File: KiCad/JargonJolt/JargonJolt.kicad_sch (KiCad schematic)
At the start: 0 parts

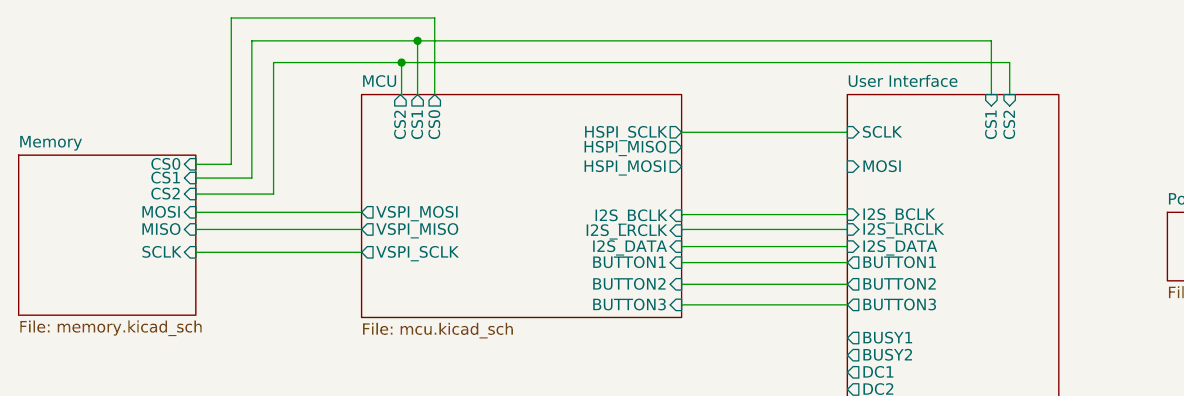
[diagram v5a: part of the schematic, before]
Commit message: added sd module + fixed CS pins
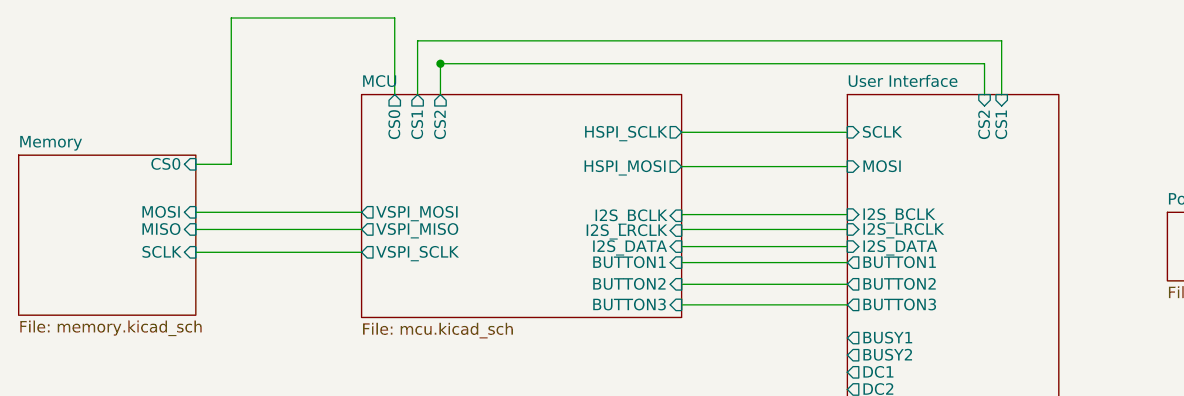
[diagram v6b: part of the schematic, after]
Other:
- sheet MCU ports: added none; removed HSPI_MISO
- sheet Memory ports: added none; removed CS1, CS2
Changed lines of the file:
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@@
 (kicad_sch (version 20230121) (generator eeschema)
   (paper "A4")
-  (junction (at 104.14 80.518) (diameter 0) (color 0 0 0 0)
-  )
-  (junction (at 105.918 78.105) (diameter 0) (color 0 0 0 0)
+  (junction (at 108.458 80.645) (diameter 0) (color 0 0 0 0)
   )
   (wire (pts (xy 135.255 97.409) (xy 153.67 97.409))
     (stroke (width 0) (type default))
   )
-  (wire (pts (xy 104.14 84.074) (xy 104.013 84.074))
+  (wire (pts (xy 108.458 80.645) (xy 108.458 84.074))
+    (stroke (width 0) (type default))
+  )
+  (wire (pts (xy 108.458 80.518) (xy 108.458 80.645))
+    (stroke (width 0) (type default))
+  )
+  (wire (pts (xy 135.255 92.075) (xy 153.67 92.075))
     (stroke (width 0) (type default))
   )
@@
     (stroke (width 0) (type default))
   )
-  (wire (pts (xy 89.916 80.518) (xy 89.916 95.123))
+  (wire (pts (xy 168.91 80.645) (xy 108.458 80.645))
     (stroke (width 0) (type default))
   )
@@
     (stroke (width 0) (type default))
   )
-  (wire (pts (xy 104.14 80.518) (xy 104.14 84.074))
-    (stroke (width 0) (type default))
-  )
   (wire (pts (xy 135.255 99.06) (xy 135.255 99.187))
     (stroke (width 0) (type default))
   )
-  (wire (pts (xy 87.503 93.345) (xy 81.28 93.345))
-    (stroke (width 0) (type default))
-  )
-  (wire (pts (xy 107.823 75.565) (xy 107.823 84.074))
+  (wire (pts (xy 103.378 75.565) (xy 103.378 84.074))
     (stroke (width 0) (type default))
   )
@@
     (stroke (width 0) (type default))
   )
+  (wire (pts (xy 168.91 80.645) (xy 168.91 84.074))
+    (stroke (width 0) (type default))
+  )
   (wire (pts (xy 135.255 99.06) (xy 153.67 99.06))
     (stroke (width 0) (type default))
   )
-  (wire (pts (xy 104.14 80.518) (xy 89.916 80.518))
-    (stroke (width 0) (type default))
-  )
-  (wire (pts (xy 169.672 84.074) (xy 169.672 78.105))
-    (stroke (width 0) (type default))
-  )
-  (wire (pts (xy 89.916 95.123) (xy 81.28 95.123))
+  (wire (pts (xy 170.815 84.074) (xy 170.815 78.105))
     (stroke (width 0) (type default))
   )
@@
     (stroke (width 0) (type default))
   )
-  (wire (pts (xy 169.672 78.105) (xy 105.918 78.105))
+  (wire (pts (xy 170.815 78.105) (xy 105.918 78.105))
     (stroke (width 0) (type default))
   )
@@
     (stroke (width 0) (type default))
   )
-  (wire (pts (xy 87.503 78.105) (xy 87.503 93.345))
-    (stroke (width 0) (type default))
-  )
-  (wire (pts (xy 105.918 78.105) (xy 87.503 78.105))
-    (stroke (width 0) (type default))
-  )
   (wire (pts (xy 135.255 102.743) (xy 153.67 102.743))
     (stroke (width 0) (type default))
   )
-  (wire (pts (xy 107.823 75.565) (xy 85.217 75.565))
-    (stroke (width 0) (type default))
-  )
-  (wire (pts (xy 171.704 84.074) (xy 171.704 80.518))
+  (wire (pts (xy 103.378 75.565) (xy 85.217 75.565))
     (stroke (width 0) (type default))
   )
@@
   )
   (wire (pts (xy 135.255 88.265) (xy 153.67 88.265))
-    (stroke (width 0) (type default))
-  )
-  (wire (pts (xy 171.704 80.518) (xy 104.14 80.518))
     (stroke (width 0) (type default))
   )
@@
       (effects (font (size 1.27 1.27)) (justify left))
     )
-    (pin "CS1" input (at 169.672 84.074 90)
-      (effects (font (size 1.27 1.27)) (justify right))
-    )
-    (pin "CS2" input (at 171.704 84.074 90)
+    (pin "CS1" input (at 170.815 84.074 90)
+      (effects (font (size 1.27 1.27)) (justify right))
+    )
+    (pin "CS2" input (at 168.91 84.074 90)
       (effects (font (size 1.27 1.27)) (justify right))
     )
@@
       (effects (font (size 1.27 1.27)) (justify right))
     )
-    (pin "CS1" input (at 81.28 93.345 0)
-      (effects (font (size 1.27 1.27)) (justify right))
-    )
-    (pin "CS2" input (at 81.28 95.123 0)
-      (effects (font (size 1.27 1.27)) (justify right))
-    )
     (pin "MOSI" input (at 81.28 97.155 0)
       (effects (font (size 1.27 1.27)) (justify right))
@@
       (effects (font (size 1.27 1.27)) (justify right))
     )
-    (pin "HSPI_MISO" output (at 135.255 89.916 0)
-      (effects (font (size 1.27 1.27)) (justify right))
-    )
     (pin "I2S_BCLK" input (at 135.255 97.536 0)
       (effects (font (size 1.27 1.27)) (justify right))
@@
       (effects (font (size 1.27 1.27)) (justify right))
     )
-    (pin "CS2" output (at 104.013 84.074 90)
+    (pin "CS2" output (at 108.458 84.074 90)
       (effects (font (size 1.27 1.27)) (justify right))
     )
@@
       (effects (font (size 1.27 1.27)) (justify right))
     )
-    (pin "CS0" output (at 107.823 84.074 90)
-      (effects (font (size 1.27 1.27)) (justify right))
-    )
+    (pin "CS0" output (at 103.378 84.074 90)
+      (effects (font (size 1.27 1.27)) (justify right))
+    )

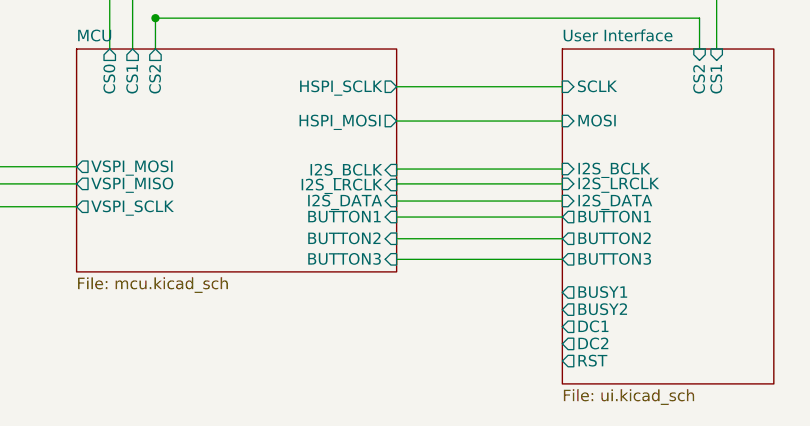
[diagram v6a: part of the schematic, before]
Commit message: added more footprints
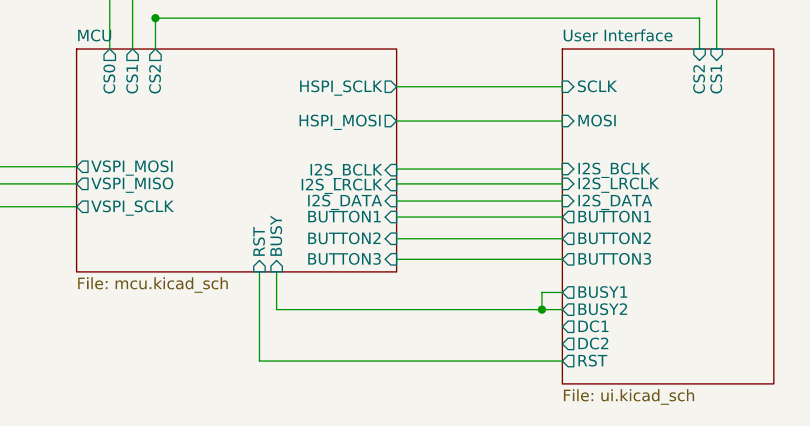
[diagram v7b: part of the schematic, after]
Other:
- sheet MCU ports: added BUSY, RST; removed none
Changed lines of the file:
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@@
   (junction (at 108.458 80.645) (diameter 0) (color 0 0 0 0)
   )
+  (junction (at 151.4031 113.03) (diameter 0) (color 0 0 0 0)
+  )
   (wire (pts (xy 135.255 97.409) (xy 153.67 97.409))
     (stroke (width 0) (type default))
@@
     (stroke (width 0) (type default))
   )
+  (wire (pts (xy 121.92 108.839) (xy 121.92 113.03))
+    (stroke (width 0) (type default))
+  )
   (wire (pts (xy 135.255 92.075) (xy 153.67 92.075))
     (stroke (width 0) (type default))
   )
+  (wire (pts (xy 151.4031 111.125) (xy 151.4031 113.03))
+    (stroke (width 0) (type default))
+  )
+  (wire (pts (xy 120.015 108.839) (xy 120.015 118.745))
+    (stroke (width 0) (type default))
+  )
   (wire (pts (xy 85.217 91.821) (xy 81.28 91.821))
     (stroke (width 0) (type default))
@@
     (stroke (width 0) (type default))
   )
+  (wire (pts (xy 151.4031 113.03) (xy 153.67 113.03))
+    (stroke (width 0) (type default))
+  )
   (wire (pts (xy 170.815 84.074) (xy 170.815 78.105))
     (stroke (width 0) (type default))
@@
     (stroke (width 0) (type default))
   )
+  (wire (pts (xy 120.015 118.745) (xy 153.67 118.745))
+    (stroke (width 0) (type default))
+  )
   (wire (pts (xy 135.255 97.409) (xy 135.255 97.536))
     (stroke (width 0) (type default))
@@
     (stroke (width 0) (type default))
   )
+  (wire (pts (xy 153.67 111.125) (xy 151.4031 111.125))
+    (stroke (width 0) (type default))
+  )
   (wire (pts (xy 135.255 88.265) (xy 153.67 88.265))
+    (stroke (width 0) (type default))
+  )
+  (wire (pts (xy 121.92 113.03) (xy 151.4031 113.03))
     (stroke (width 0) (type default))
   )
@@
       (effects (font (size 1.27 1.27)) (justify right))
     )
-    (instances
+    (pin "RST" input (at 120.015 108.839 270)
+      (effects (font (size 1.27 1.27)) (justify left))
+    )
+    (pin "BUSY" input (at 121.92 108.839 270)
+      (effects (font (size 1.27 1.27)) (justify left))
+    )
+    (instances

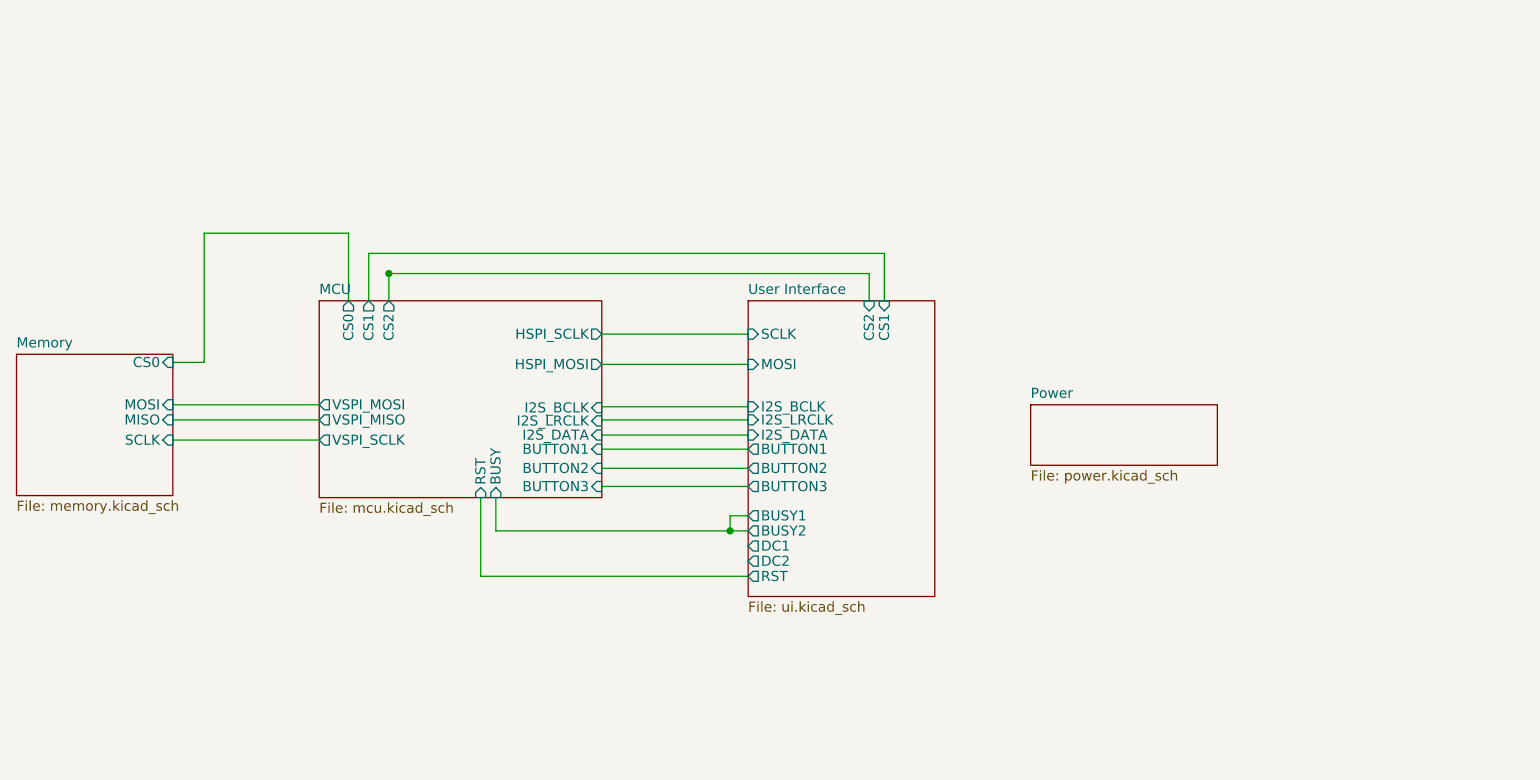
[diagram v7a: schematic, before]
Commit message: PCB first revision
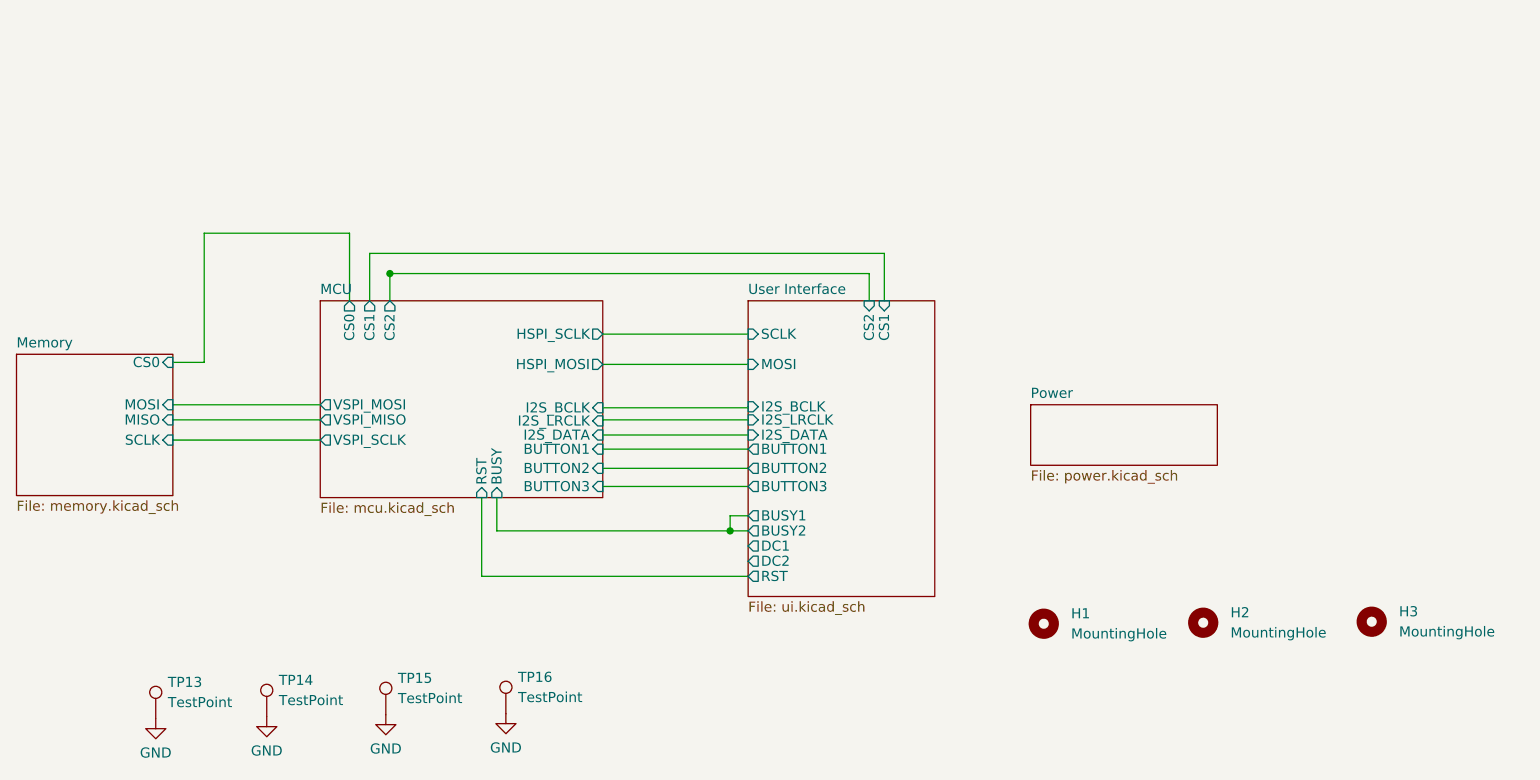
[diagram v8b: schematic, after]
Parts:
- added H1, H2, H3: MountingHole, MountingHole:MountingHole_2.2mm_M2, symbol Mechanical:MountingHole
- added TP13, TP14, TP15, TP16: TestPoint, TestPoint:TestPoint_Pad_D1.5mm, symbol Connector:TestPoint
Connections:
- new net GND: TP13.1, TP14.1, TP15.1, TP16.1
